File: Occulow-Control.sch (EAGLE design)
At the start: 21 parts, among them J1 CORTEX_DEBUG_PTH, T1 DMP3010LK3, T2 DMP3010LK3, T3 DMP3010LK3

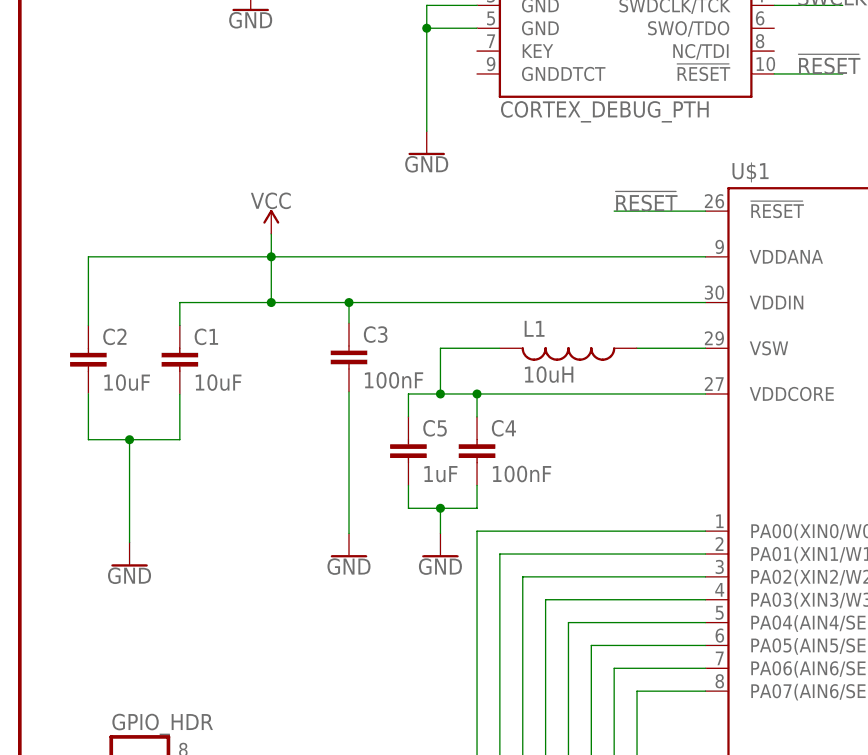
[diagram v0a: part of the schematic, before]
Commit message: Fixed power filtering circuit
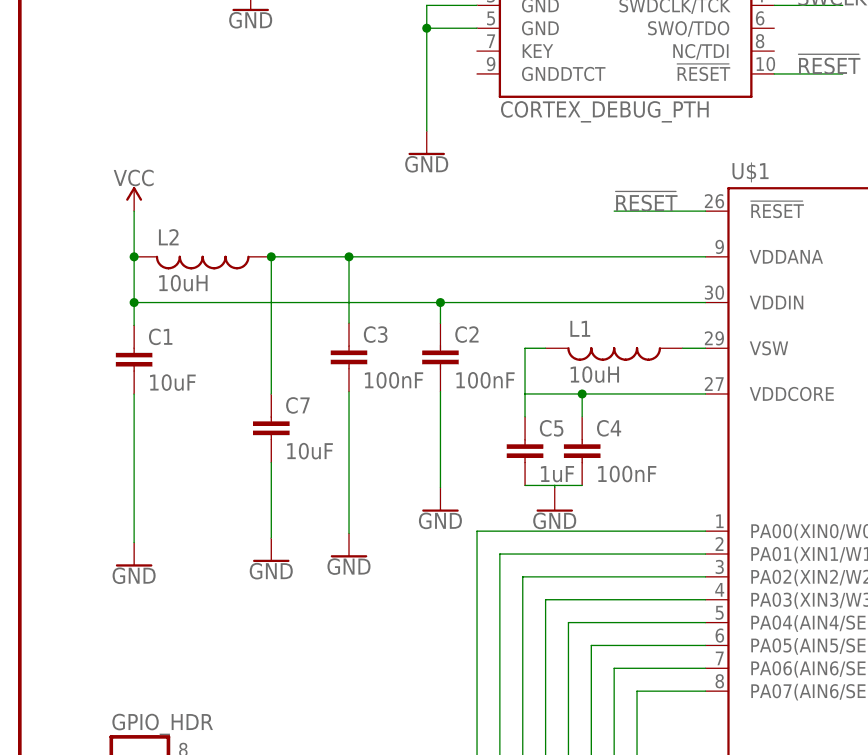
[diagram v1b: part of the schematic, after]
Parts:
- added C7: 10uF, rcl:C-EUC1206
- added L2: 10uH, resistor:L-USL2012C
- C2: value 10uF -> 100nF
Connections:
- new net N$12: C3.1, C7.1, L2.1, U$1.VDDANA
- net GND: now also C7.2
- net VCC: now also L2.2; no longer C3.1, U$1.VDDANA
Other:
- moved on the sheet: C1, C2, C4, C5, L1
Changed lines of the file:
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@@
 <?xml version="1.0" encoding="utf-8"?>
 <!DOCTYPE eagle SYSTEM "eagle.dtd">
-<eagle version="8.0.2">
+<eagle version="8.1.0">
 <drawing>
 <settings>
@@
 <part name="GND1" library="SparkFun-PowerSymbols" deviceset="GND" device=""/>
 <part name="SUPPLY1" library="SparkFun-PowerSymbols" deviceset="VCC" device=""/>
-<part name="C2" library="rcl" deviceset="C-EU" device="C1206" value="10uF"/>
 <part name="C3" library="rcl" deviceset="C-EU" device="C1206" value="100nF"/>
 <part name="C4" library="rcl" deviceset="C-EU" device="C1206" value="100nF"/>
 <part name="C5" library="rcl" deviceset="C-EU" device="C1206" value="1uF"/>
-<part name="GND4" library="SparkFun-PowerSymbols" deviceset="GND" device=""/>
 <part name="GND2" library="SparkFun-PowerSymbols" deviceset="GND" device=""/>
 <part name="GND3" library="SparkFun-PowerSymbols" deviceset="GND" device=""/>
@@
 <part name="SL1" library="con-amp-quick" deviceset="M06" device=""/>
 <part name="L1" library="resistor" deviceset="L-US" device="L2012C" value="10uH"/>
+<part name="L2" library="resistor" deviceset="L-US" device="L2012C" value="10uH"/>
+<part name="C7" library="rcl" deviceset="C-EU" device="C1206" value="10uF"/>
+<part name="GND12" library="SparkFun-PowerSymbols" deviceset="GND" device=""/>
+<part name="C2" library="rcl" deviceset="C-EU" device="C1206" value="100nF"/>
+<part name="GND4" library="SparkFun-PowerSymbols" deviceset="GND" device=""/>
+<part name="GND13" library="SparkFun-PowerSymbols" deviceset="GND" device=""/>
 </parts>
 <sheets>
@@
 <instance part="FRAME1" gate="V" x="147.32" y="0"/>
 <instance part="U$1" gate="G$1" x="109.22" y="63.5"/>
-<instance part="C1" gate="G$1" x="17.78" y="81.28"/>
+<instance part="C1" gate="G$1" x="12.7" y="81.28"/>
 <instance part="GND1" gate="1" x="73.66" y="20.32"/>
-<instance part="SUPPLY1" gate="G$1" x="27.94" y="93.98"/>
-<instance part="C2" gate="G$1" x="7.62" y="81.28"/>
+<instance part="SUPPLY1" gate="G$1" x="12.7" y="96.52"/>
 <instance part="C3" gate="G$1" x="36.576" y="81.534"/>
-<instance part="C4" gate="G$1" x="50.8" y="71.12"/>
-<instance part="C5" gate="G$1" x="43.18" y="71.12"/>
-<instance part="GND4" gate="1" x="46.736" y="58.166"/>
-<instance part="GND2" gate="1" x="12.192" y="57.15"/>
+<instance part="C4" gate="G$1" x="62.484" y="71.12"/>
+<instance part="C5" gate="G$1" x="56.134" y="71.12"/>
+<instance part="GND2" gate="1" x="12.7" y="57.15"/>
 <instance part="GND3" gate="1" x="36.576" y="58.166"/>
 <instance part="U$2" gate="G$1" x="195.58" y="116.84"/>
@@
 <instance part="GND11" gate="1" x="25.654" y="118.872"/>
 <instance part="SL1" gate="G$1" x="139.7" y="149.86" rot="R180"/>
-<instance part="L1" gate="G$1" x="60.96" y="81.28" rot="R270"/>
+<instance part="L1" gate="G$1" x="66.04" y="81.28" rot="R270"/>
+<instance part="L2" gate="G$1" x="20.32" y="91.44" rot="R270"/>
+<instance part="C7" gate="G$1" x="27.94" y="73.66"/>
+<instance part="GND12" gate="1" x="27.94" y="57.658"/>
+<instance part="C2" gate="G$1" x="46.736" y="81.534"/>
+<instance part="GND4" gate="1" x="59.436" y="63.246"/>
+<instance part="GND13" gate="1" x="46.736" y="63.246"/>
 </instances>
 <busses>
@@
 <junction x="73.66" y="30.48"/>
 <pinref part="GND1" gate="1" pin="GND"/>
-</segment>
-<segment>
-<pinref part="C5" gate="G$1" pin="2"/>
-<wire x1="43.18" y1="66.04" x2="43.18" y2="63.5" width="0.1524" layer="91"/>
-<pinref part="C4" gate="G$1" pin="2"/>
-<wire x1="50.8" y1="66.04" x2="50.8" y2="63.5" width="0.1524" layer="91"/>
-<wire x1="50.8" y1="63.5" x2="46.736" y2="63.5" width="0.1524" layer="91"/>
-<pinref part="GND4" gate="1" pin="GND"/>
-<wire x1="46.736" y1="63.5" x2="43.18" y2="63.5" width="0.1524" layer="91"/>
-<wire x1="46.736" y1="60.706" x2="46.736" y2="63.5" width="0.1524" layer="91"/>
-<junction x="46.736" y="63.5"/>
-</segment>
-<segment>
-<pinref part="C1" gate="G$1" pin="2"/>
-<wire x1="17.78" y1="76.2" x2="17.78" y2="71.12" width="0.1524" layer="91"/>
-<pinref part="C2" gate="G$1" pin="2"/>
-<wire x1="7.62" y1="76.2" x2="7.62" y2="71.12" width="0.1524" layer="91"/>
-<wire x1="17.78" y1="71.12" x2="12.192" y2="71.12" width="0.1524" layer="91"/>
-<pinref part="GND2" gate="1" pin="GND"/>
-<wire x1="12.192" y1="71.12" x2="7.62" y2="71.12" width="0.1524" layer="91"/>
-<wire x1="12.192" y1="59.69" x2="12.192" y2="71.12" width="0.1524" layer="91"/>
-<junction x="12.192" y="71.12"/>
 </segment>
 <segment>
@@
 <wire x1="118.872" y1="152.4" x2="118.872" y2="148.59" width="0.1524" layer="91"/>
 </segment>
+<segment>
+<pinref part="C7" gate="G$1" pin="2"/>
+<pinref part="GND12" gate="1" pin="GND"/>
+<wire x1="27.94" y1="68.58" x2="27.94" y2="60.198" width="0.1524" layer="91"/>
+</segment>
+<segment>
+<pinref part="GND2" gate="1" pin="GND"/>
+<pinref part="C1" gate="G$1" pin="2"/>
+<wire x1="12.7" y1="59.69" x2="12.7" y2="76.2" width="0.1524" layer="91"/>
+</segment>
+<segment>
+<pinref part="C5" gate="G$1" pin="2"/>
+<pinref part="GND4" gate="1" pin="GND"/>
+<wire x1="56.134" y1="66.04" x2="59.436" y2="66.04" width="0.1524" layer="91"/>
+<pinref part="C4" gate="G$1" pin="2"/>
+<wire x1="62.484" y1="66.04" x2="59.436" y2="66.04" width="0.1524" layer="91"/>
+<wire x1="59.436" y1="66.04" x2="59.436" y2="65.786" width="0.1524" layer="91"/>
+</segment>
+<segment>
+<pinref part="C2" gate="G$1" pin="2"/>
+<pinref part="GND13" gate="1" pin="GND"/>
+<wire x1="46.736" y1="76.454" x2="46.736" y2="65.786" width="0.1524" layer="91"/>
+</segment>
 </net>
 <net name="VCC" class="0">
 <segment>
+<pinref part="SUPPLY1" gate="G$1" pin="VCC"/>
+<wire x1="12.7" y1="96.52" x2="12.7" y2="91.44" width="0.1524" layer="91"/>
+<pinref part="L2" gate="G$1" pin="2"/>
+<pinref part="C1" gate="G$1" pin="1"/>
 <pinref part="U$1" gate="G$1" pin="VDDIN"/>
-<pinref part="C1" gate="G$1" pin="1"/>
-<wire x1="76.2" y1="86.36" x2="36.576" y2="86.36" width="0.1524" layer="91"/>
-<wire x1="36.576" y1="86.36" x2="27.94" y2="86.36" width="0.1524" layer="91"/>
-<wire x1="27.94" y1="86.36" x2="17.78" y2="86.36" width="0.1524" layer="91"/>
-<wire x1="17.78" y1="86.36" x2="17.78" y2="83.82" width="0.1524" layer="91"/>
-<pinref part="SUPPLY1" gate="G$1" pin="VCC"/>
-<wire x1="27.94" y1="93.98" x2="27.94" y2="91.44" width="0.1524" layer="91"/>
-<junction x="27.94" y="86.36"/>
-<pinref part="U$1" gate="G$1" pin="VDDANA"/>
-<wire x1="27.94" y1="91.44" x2="27.94" y2="86.36" width="0.1524" layer="91"/>
-<wire x1="76.2" y1="91.44" x2="27.94" y2="91.44" width="0.1524" layer="91"/>
-<junction x="27.94" y="91.44"/>
+<wire x1="76.2" y1="86.36" x2="46.736" y2="86.36" width="0.1524" layer="91"/>
+<wire x1="46.736" y1="86.36" x2="12.7" y2="86.36" width="0.1524" layer="91"/>
+<wire x1="12.7" y1="86.36" x2="12.7" y2="83.82" width="0.1524" layer="91"/>
+<wire x1="12.7" y1="91.44" x2="12.7" y2="86.36" width="0.1524" layer="91"/>
+<junction x="12.7" y="91.44"/>
+<junction x="12.7" y="86.36"/>
 <pinref part="C2" gate="G$1" pin="1"/>
-<wire x1="27.94" y1="91.44" x2="7.62" y2="91.44" width="0.1524" layer="91"/>
-<wire x1="7.62" y1="91.44" x2="7.62" y2="83.82" width="0.1524" layer="91"/>
-<pinref part="C3" gate="G$1" pin="1"/>
-<wire x1="36.576" y1="84.074" x2="36.576" y2="86.36" width="0.1524" layer="91"/>
-<junction x="36.576" y="86.36"/>
+<wire x1="46.736" y1="84.074" x2="46.736" y2="86.36" width="0.1524" layer="91"/>
+<junction x="46.736" y="86.36"/>
 </segment>
 <segment>
@@
 </segment>
 </net>
-<net name="N$1" class="0">
-<segment>
-<pinref part="U$1" gate="G$1" pin="VDDCORE"/>
-<pinref part="C4" gate="G$1" pin="1"/>
-<wire x1="76.2" y1="76.2" x2="50.8" y2="76.2" width="0.1524" layer="91"/>
-<wire x1="50.8" y1="76.2" x2="50.8" y2="73.66" width="0.1524" layer="91"/>
-<pinref part="C5" gate="G$1" pin="1"/>
-<wire x1="50.8" y1="76.2" x2="46.736" y2="76.2" width="0.1524" layer="91"/>
-<wire x1="46.736" y1="76.2" x2="43.18" y2="76.2" width="0.1524" layer="91"/>
-<wire x1="43.18" y1="76.2" x2="43.18" y2="73.66" width="0.1524" layer="91"/>
-<junction x="50.8" y="76.2"/>
-<pinref part="L1" gate="G$1" pin="2"/>
-<wire x1="53.34" y1="81.28" x2="46.736" y2="81.28" width="0.1524" layer="91"/>
-<wire x1="46.736" y1="81.28" x2="46.736" y2="76.2" width="0.1524" layer="91"/>
-<junction x="46.736" y="76.2"/>
-</segment>
-</net>
 <net name="RF" class="0">
 <segment>
@@
 <pinref part="U$1" gate="G$1" pin="VSW"/>
 <pinref part="L1" gate="G$1" pin="1"/>
-<wire x1="76.2" y1="81.28" x2="68.58" y2="81.28" width="0.1524" layer="91"/>
-</segment>
-</net>
+<wire x1="76.2" y1="81.28" x2="73.66" y2="81.28" width="0.1524" layer="91"/>
+</segment>
+</net>
+<net name="N$12" class="0">
+<segment>
+<pinref part="L2" gate="G$1" pin="1"/>
+<pinref part="U$1" gate="G$1" pin="VDDANA"/>
+<wire x1="27.94" y1="91.44" x2="36.576" y2="91.44" width="0.1524" layer="91"/>
+<wire x1="36.576" y1="91.44" x2="76.2" y2="91.44" width="0.1524" layer="91"/>
+<wire x1="27.94" y1="91.44" x2="27.94" y2="76.2" width="0.1524" layer="91"/>
+<junction x="27.94" y="91.44"/>
+<pinref part="C7" gate="G$1" pin="1"/>
+<pinref part="C3" gate="G$1" pin="1"/>
+<wire x1="36.576" y1="84.074" x2="36.576" y2="91.44" width="0.1524" layer="91"/>
+<junction x="36.576" y="91.44"/>
+</segment>
+</net>
+<net name="N$1" class="0">
+<segment>
+<pinref part="L1" gate="G$1" pin="2"/>
+<pinref part="C5" gate="G$1" pin="1"/>
+<wire x1="58.42" y1="81.28" x2="56.134" y2="81.28" width="0.1524" layer="91"/>
+<wire x1="56.134" y1="81.28" x2="56.134" y2="76.2" width="0.1524" layer="91"/>
+<pinref part="U$1" gate="G$1" pin="VDDCORE"/>
+<wire x1="56.134" y1="76.2" x2="56.134" y2="73.66" width="0.1524" layer="91"/>
+<wire x1="76.2" y1="76.2" x2="62.484" y2="76.2" width="0.1524" layer="91"/>
+<wire x1="62.484" y1="76.2" x2="56.134" y2="76.2" width="0.1524" layer="91"/>
+<pinref part="C4" gate="G$1" pin="1"/>
+<wire x1="62.484" y1="73.66" x2="62.484" y2="76.2" width="0.1524" layer="91"/>
+<junction x="62.484" y="76.2"/>
+</segment>
+</net>

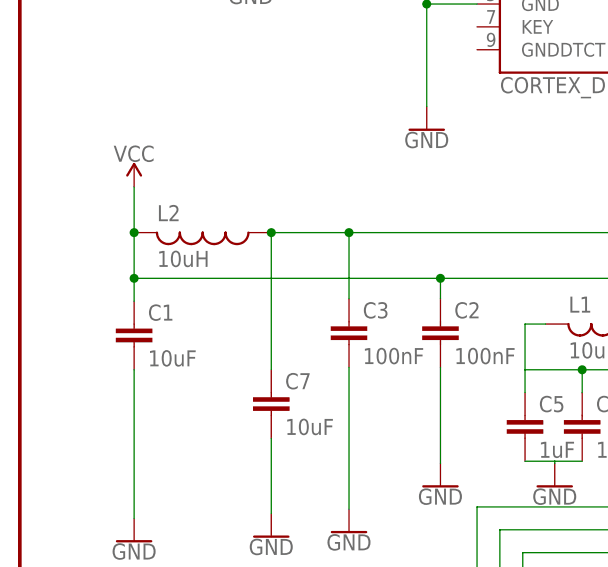
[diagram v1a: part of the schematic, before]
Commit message: Ferrite bead, changed inductor package
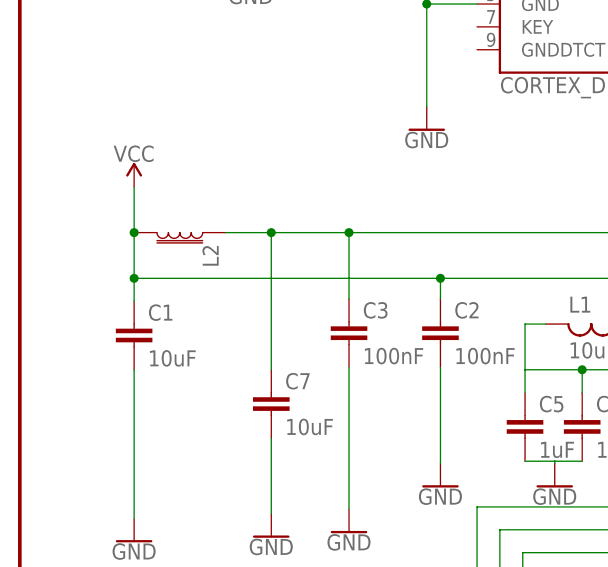
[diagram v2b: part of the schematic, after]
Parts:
- L1: device resistor:L-USL2012C -> resistor:L-USL3225M
- L2: value 10uH -> FERRITE_BEAD-0603; device resistor:L-USL2012C -> SparkFun-Coils:FERRITE_BEAD-0603
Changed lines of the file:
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@@
 <?xml version="1.0" encoding="utf-8"?>
 <!DOCTYPE eagle SYSTEM "eagle.dtd">
-<eagle version="8.1.0">
+<eagle version="8.0.2">
 <drawing>
 <settings>
@@
 <part name="GND11" library="SparkFun-PowerSymbols" deviceset="GND" device=""/>
 <part name="SL1" library="con-amp-quick" deviceset="M06" device=""/>
-<part name="L1" library="resistor" deviceset="L-US" device="L2012C" value="10uH"/>
-<part name="L2" library="resistor" deviceset="L-US" device="L2012C" value="10uH"/>
+<part name="L1" library="resistor" deviceset="L-US" device="L3225M" value="10uH"/>
+<part name="L2" library="SparkFun-Coils" deviceset="FERRITE_BEAD" device="-0603" value=""/>
 <part name="C7" library="rcl" deviceset="C-EU" device="C1206" value="10uF"/>
 <part name="GND12" library="SparkFun-PowerSymbols" deviceset="GND" device=""/>
@@
 <instance part="SL1" gate="G$1" x="139.7" y="149.86" rot="R180"/>
 <instance part="L1" gate="G$1" x="66.04" y="81.28" rot="R270"/>
-<instance part="L2" gate="G$1" x="20.32" y="91.44" rot="R270"/>
+<instance part="L2" gate="G$1" x="17.78" y="91.44" rot="R270"/>
 <instance part="C7" gate="G$1" x="27.94" y="73.66"/>
 <instance part="GND12" gate="1" x="27.94" y="57.658"/>
@@
 <pinref part="L2" gate="G$1" pin="1"/>
 <pinref part="U$1" gate="G$1" pin="VDDANA"/>
+<wire x1="22.86" y1="91.44" x2="27.94" y2="91.44" width="0.1524" layer="91"/>
 <wire x1="27.94" y1="91.44" x2="36.576" y2="91.44" width="0.1524" layer="91"/>
 <wire x1="36.576" y1="91.44" x2="76.2" y2="91.44" width="0.1524" layer="91"/>
-<wire x1="27.94" y1="91.44" x2="27.94" y2="76.2" width="0.1524" layer="91"/>
-<junction x="27.94" y="91.44"/>
-<pinref part="C7" gate="G$1" pin="1"/>
 <pinref part="C3" gate="G$1" pin="1"/>
 <wire x1="36.576" y1="84.074" x2="36.576" y2="91.44" width="0.1524" layer="91"/>
 <junction x="36.576" y="91.44"/>
-</segment>
-</net>
+<pinref part="C7" gate="G$1" pin="1"/>
+<wire x1="27.94" y1="76.2" x2="27.94" y2="91.44" width="0.1524" layer="91"/>
+<junction x="27.94" y="91.44"/>
+</segment>
+</net>
